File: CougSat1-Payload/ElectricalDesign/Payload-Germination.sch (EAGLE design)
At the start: 0 parts

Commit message: added buffers
not wired yet
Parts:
- added J1: CougSat Socket, CougsInSpace-Connectors:CIS_CARD-PCIE
- added J2: (no value), CougsInSpace-Connectors:1X10-PICOLOCK
- added Q1, Q2: CSD25402Q3A, CougsInSpace-DiscreteSemi:MOSFET-P-SON-3333
- added U1, U2, U3: TXS0102DQM, CougsInSpace-IC-Comms:LEVEL_SHIFTER-2BIT-XSON-8
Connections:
- new net 3.3V_7: J1POWER.PR_3.3V-7, Q2.S
- new net 3.3V_8: J1POWER.PR_3.3V-8, J2.8
- new net HEATER: J2.9, Q1.D
- new net HEAT_CONTROL: Q1.G
- new net I2C_SCL: J1DATA.BUS_I2C0_SCL, J2.2
- new net I2C_SCLL: U1.A1
- new net I2C_SDA: J1DATA.BUS_I2C0_SDA, J2.1
- new net LIGHT: J2.7, Q2.D
- new net LIGHT_CONTROL: Q2.G
- new net N$2: U1.A2
- new net PGND: J2.10
- new net SPI_CS: J2.6
- new net SPI_MISO: J1DATA.BUS_SPI_MISO, J2.4
- new net SPI_MOSI: J1DATA.BUS_SPI_MOSI, J2.5
- new net SPI_SCK: J1DATA.BUS_SPI_SCK, J2.3
- new net VBATT_0: J1POWER.PR_BATT-0, Q1.S

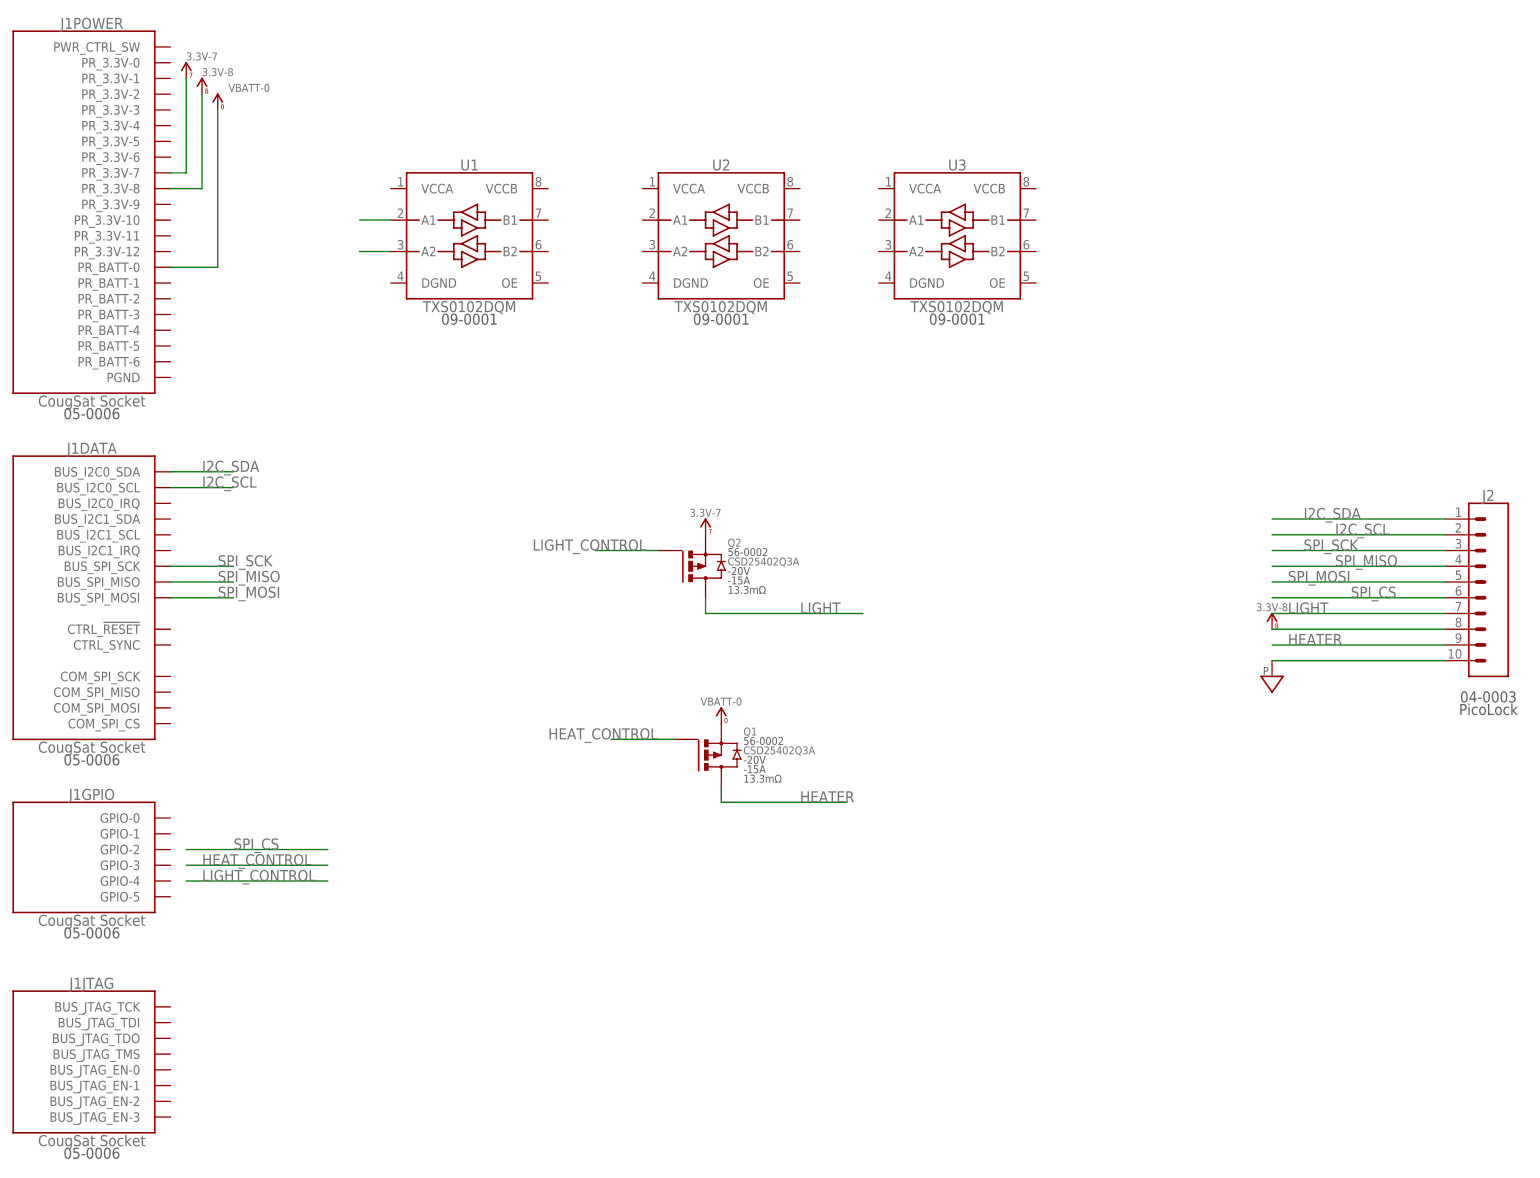
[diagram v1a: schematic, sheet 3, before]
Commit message: Updated buffer connections
Connected SPI and I2C to buffers
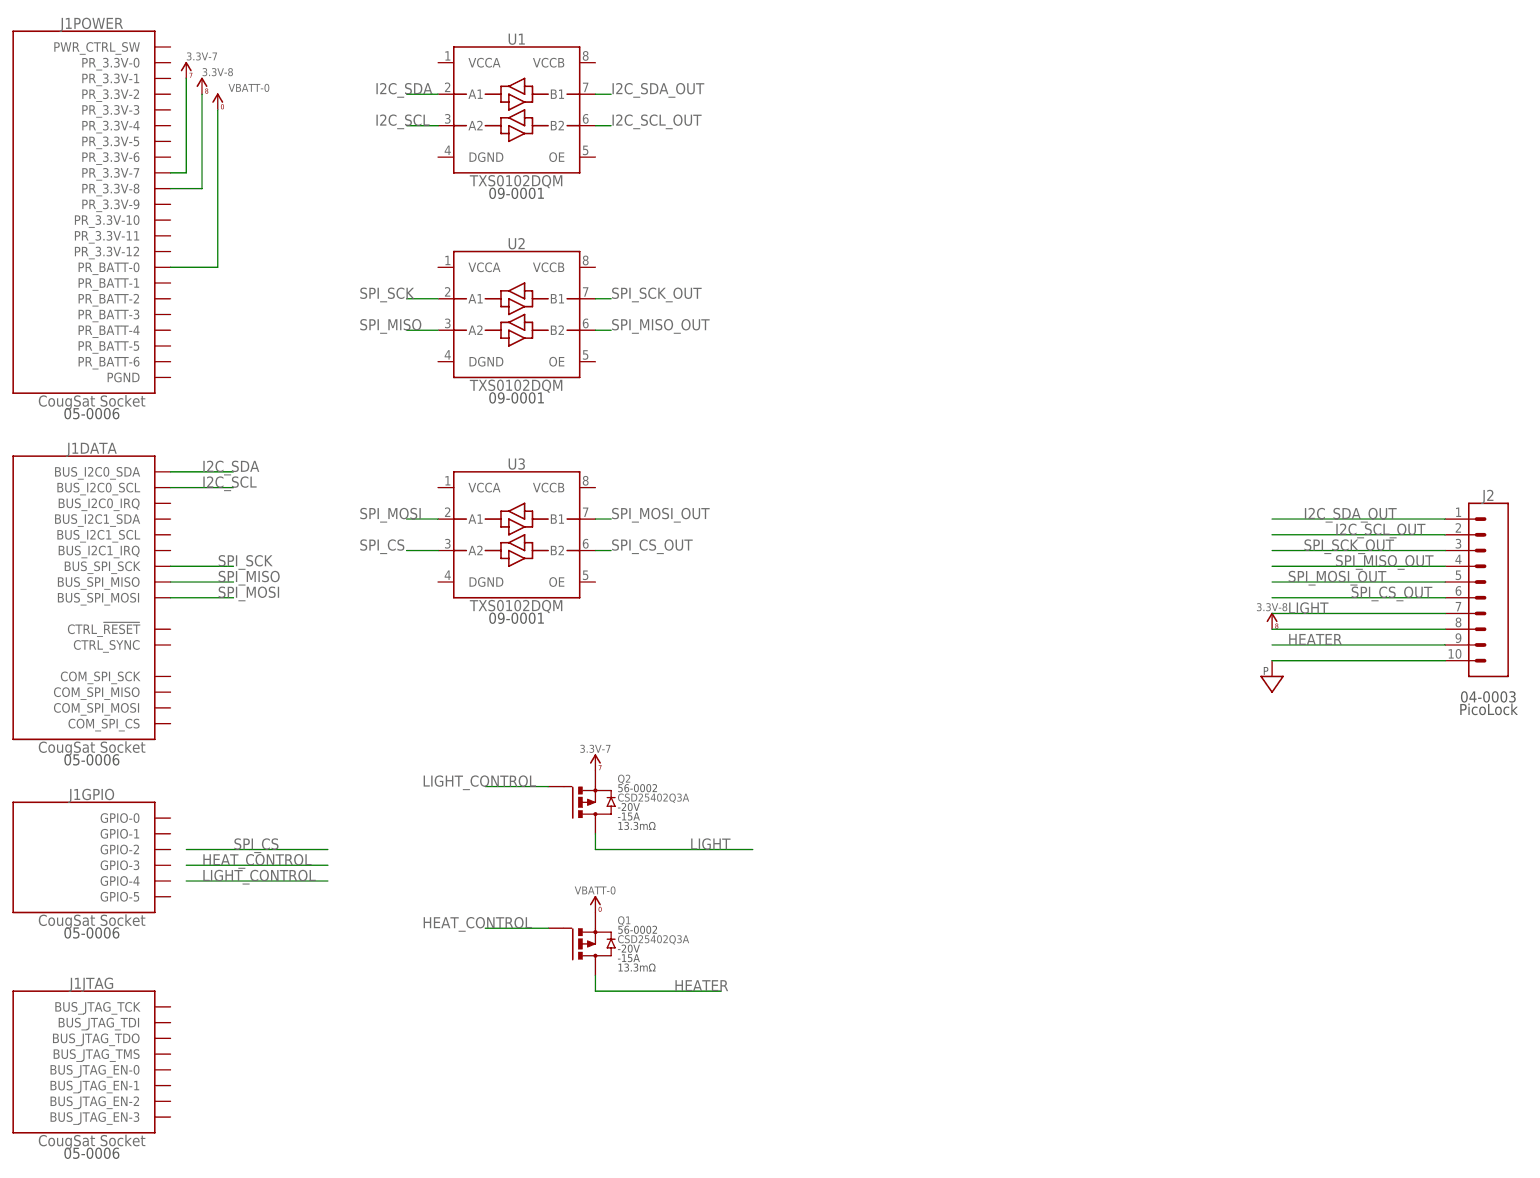
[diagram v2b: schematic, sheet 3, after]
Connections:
- removed net I2C_SCLL: U1.A1
- removed net N$2: U1.A2
- new net I2C_SCL_OUT: J2.2, U1.B2
- new net I2C_SDA_OUT: J2.1, U1.B1
- new net SPI_CS_OUT: J2.6, U3.B2
- new net SPI_MISO_OUT: J2.4, U2.B2
- new net SPI_MOSI_OUT: J2.5, U3.B1
- new net SPI_SCK_OUT: J2.3, U2.B1
- net I2C_SCL: now also U1.A2; no longer J2.2
- net I2C_SDA: now also U1.A1; no longer J2.1
- net SPI_CS: now also U3.A2; no longer J2.6
- net SPI_MISO: now also U2.A2; no longer J2.4
- net SPI_MOSI: now also U3.A1; no longer J2.5
- net SPI_SCK: now also U2.A1; no longer J2.3
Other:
- moved on the sheet: Q1, Q2, U1, U2, U3

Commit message: Revert "Updated buffer connections"
This reverts commit 97c00d36a388c3aa67f6eef2402791ba84bf0edd.
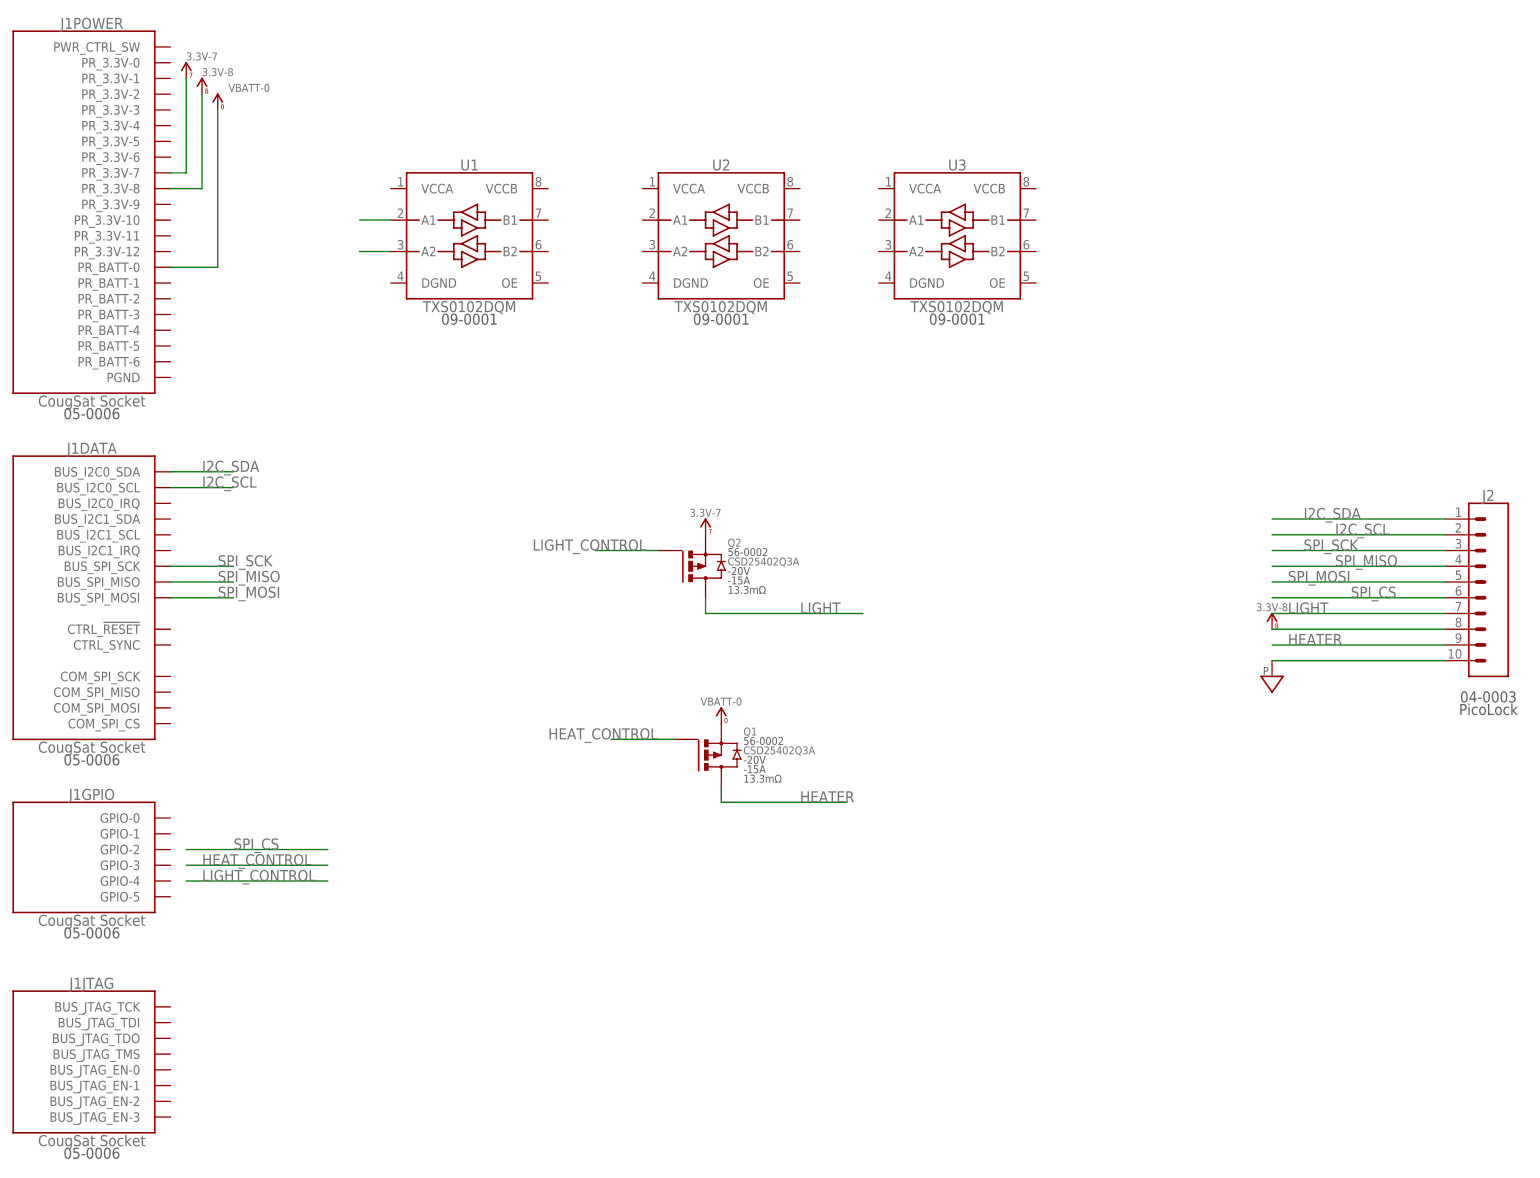
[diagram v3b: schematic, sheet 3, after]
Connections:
- removed net I2C_SCL_OUT: J2.2, U1.B2
- removed net I2C_SDA_OUT: J2.1, U1.B1
- removed net SPI_CS_OUT: J2.6, U3.B2
- removed net SPI_MISO_OUT: J2.4, U2.B2
- removed net SPI_MOSI_OUT: J2.5, U3.B1
- removed net SPI_SCK_OUT: J2.3, U2.B1
- new net I2C_SCLL: U1.A1
- new net N$2: U1.A2
- net I2C_SCL: now also J2.2; no longer U1.A2
- net I2C_SDA: now also J2.1; no longer U1.A1
- net SPI_CS: now also J2.6; no longer U3.A2
- net SPI_MISO: now also J2.4; no longer U2.A2
- net SPI_MOSI: now also J2.5; no longer U3.A1
- net SPI_SCK: now also J2.3; no longer U2.A1
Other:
- moved on the sheet: Q1, Q2, U1, U2, U3
